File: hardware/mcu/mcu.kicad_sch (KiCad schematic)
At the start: 20 parts, among them J1 PROG, U1 RP2040, U3 W25Q32JVZP, Y1 ABLS

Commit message: library updates, mcu i2c devices
added MAX31331 RTC to library, added EEPROM and RTC sub-schematic to MCU, expanded mcu planning chart
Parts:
- added C14: 1u, Capacitor_SMD:C_0603_1608Metric_Pad1.08x0.95mm_HandSolder, symbol Device:C
- added R10: 100k, Resistor_SMD:R_0402_1005Metric_Pad0.72x0.64mm_HandSolder, symbol Device:R_US
- added R8, R9: 4.7k, Resistor_SMD:R_0402_1005Metric_Pad0.72x0.64mm_HandSolder, symbol Device:R_US
- added SW1: RESET, symbol Switch:SW_Push
- C1, C12, C2, C3, C4, C5, C6, C7, C8, C9: Size (none) -> 0402; VRating (none) -> 16V
- C10, C11: footprint Capacitor_SMD:C_0402_1005Metric_Pad0.74x0.62mm_HandSolder -> Capacitor_SMD:C_0603_1608Metric_Pad1.08x0.95mm_HandSolder; Size (none) -> 0603; VRating (none) -> 16V
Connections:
- net GND: now also C2.1, U1.19 (TESTEN), C14.2, SW1.1; no longer C2.2
- net VDD: now also C14.1, R10.2, R8.2, R9.2
- net XTL_2: now also C2.2; no longer C2.1
- net at U1.26 (RUN): now also R10.1, SW1.2
- net SW renamed SWD
- new net SCL: R9.1
- new net SDA: R8.1
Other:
- added sheet EEPROM-RTC (EEPROM-RTC.kicad_sch)

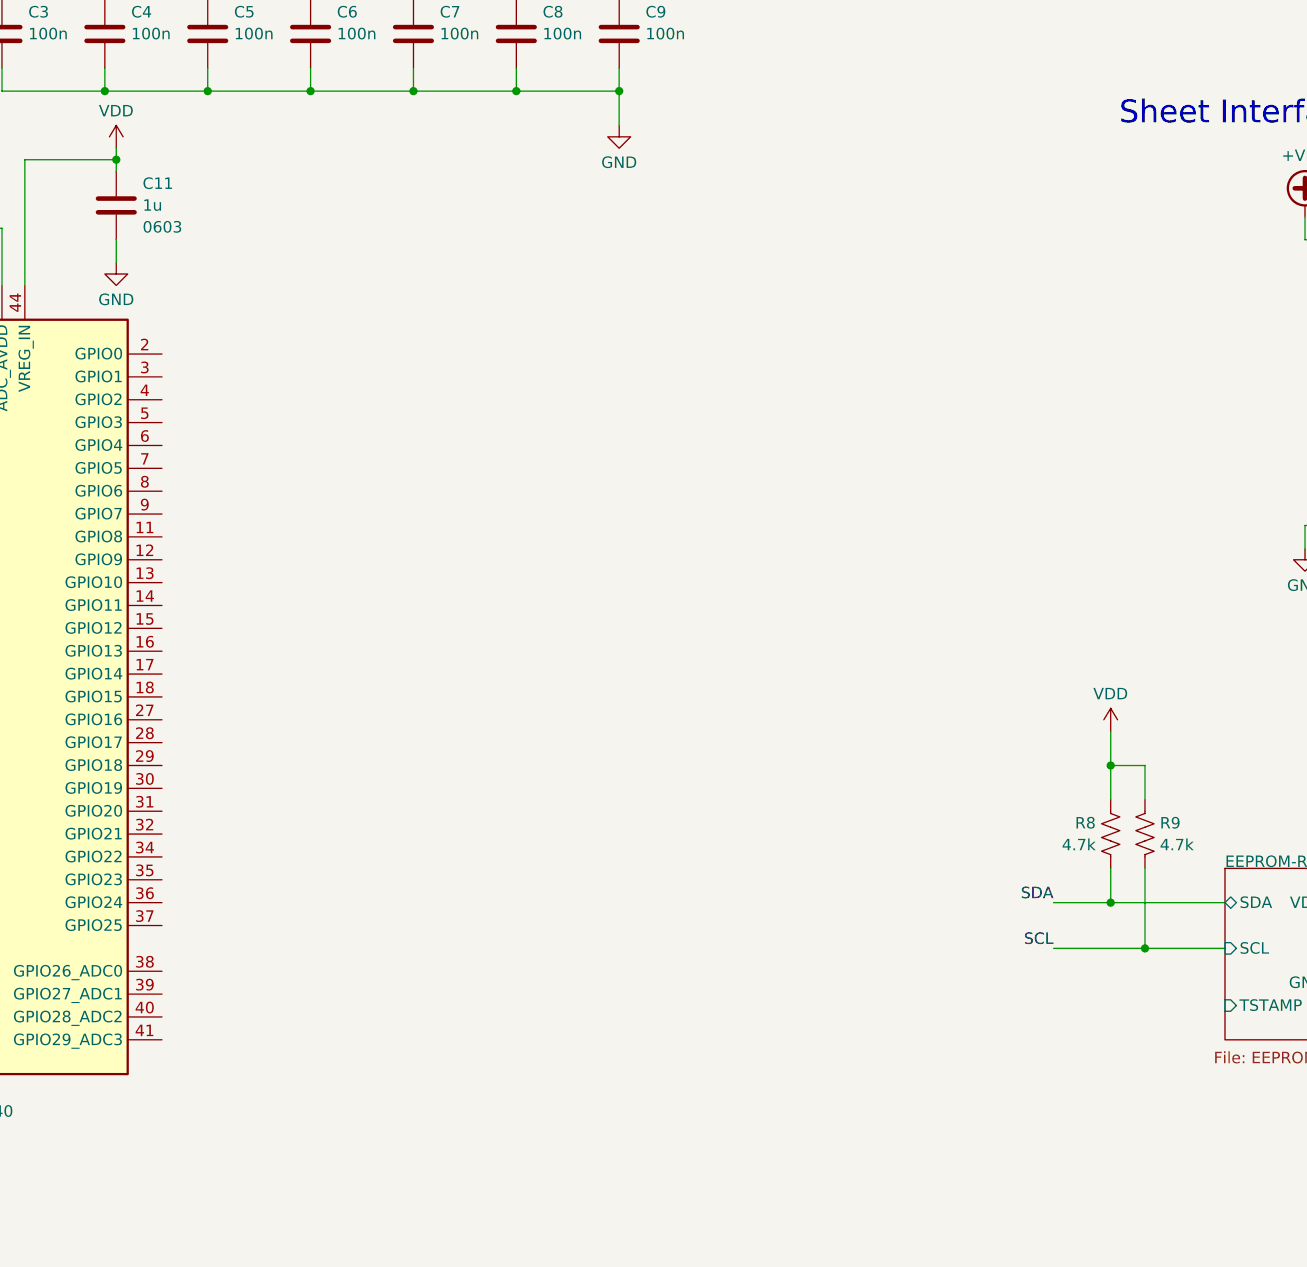
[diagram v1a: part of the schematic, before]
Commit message: I2C device notes
added notes on I2C device addresses (in-schematic)
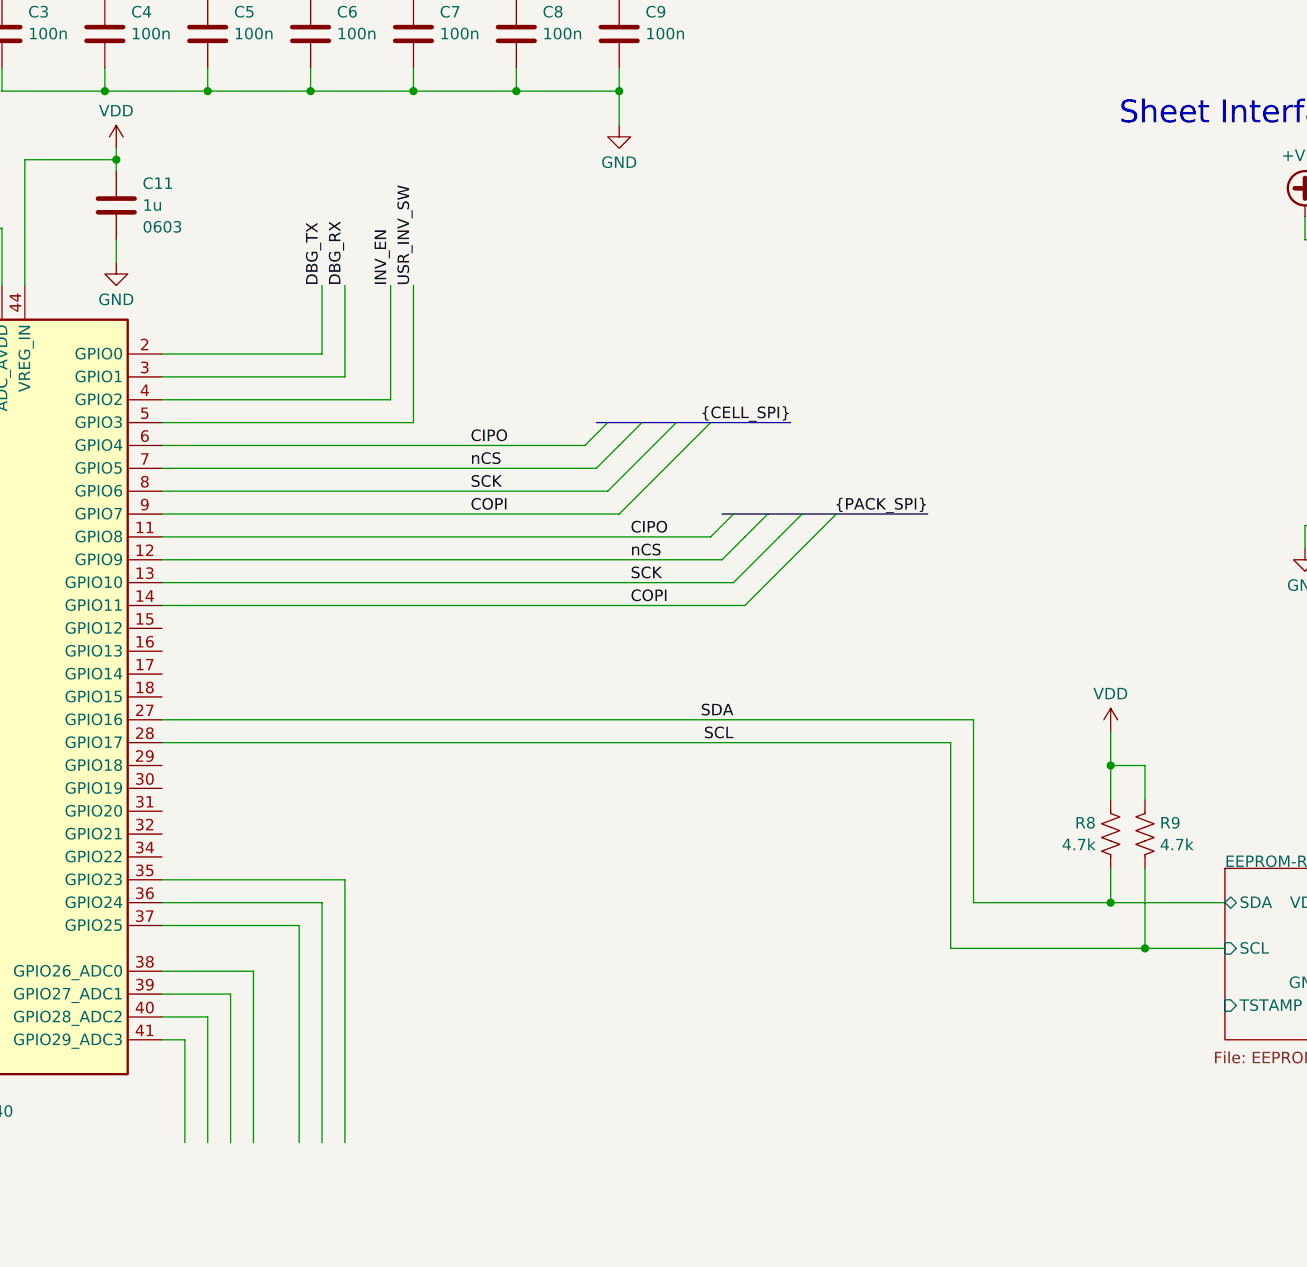
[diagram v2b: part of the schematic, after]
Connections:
- net SCL: now also U1.28 (GPIO17)
- net SDA: now also U1.27 (GPIO16)
- net CIPO: now reaches U1.11 (GPIO8)
- net CIPO: now also U1.6 (GPIO4)
- net nCS: now reaches U1.12 (GPIO9)
- net nCS: now also U1.7 (GPIO5)
- net SCK: now reaches U1.13 (GPIO10)
- net SCK: now also U1.8 (GPIO6)
- net COPI: now reaches U1.14 (GPIO11)
- net COPI: now also U1.9 (GPIO7)
- net DBG_TX: now reaches U1.2 (GPIO0)
- net DBG_RX: now reaches U1.3 (GPIO1)
- net INV_EN: now reaches U1.4 (GPIO2)
- net USR_INV_SW: now reaches U1.5 (GPIO3)

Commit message: huge update
massive update; finished lv power sys hardware design, started lv power sys mcu program
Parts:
- added J2: DEBUG, Connector_PinHeader_2.54mm:PinHeader_1x04_P2.54mm_Vertical, symbol Connector:Conn_01x04_Pin
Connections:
- net DBG_RX: now also J2.3 (Pin_3)
- net DBG_TX: now also J2.2 (Pin_2)
- net GND: now also J2.4 (Pin_4)
- net VDD: now also J2.1 (Pin_1)
- net CHG_SSR_EN: now reaches U1.15 (GPIO12)
- net BUS_SSR_EN: now reaches U1.16 (GPIO13)
- net BMS_PWR_EN: now reaches U1.17 (GPIO14)
- net MCU_RUN: now reaches R10.1, SW1.2, U1.26 (RUN)
- net LV_REG_EN: now reaches U1.29 (GPIO18)
- net TRICKLE_EN: now reaches U1.30 (GPIO19)
- net SUPV_DOUT: now reaches U1.31 (GPIO20)
- net SUPV_DIN: now reaches U1.32 (GPIO21)
- net SYS_LED: now reaches U1.34 (GPIO22)
- net USER_USB_DIR: now reaches U1.35 (GPIO23)
- net USB_BUS_EN: now reaches U1.36 (GPIO24)
- net USB_CC_DIR: now reaches U1.37 (GPIO25)
- net USBN: now reaches R4.2
- net USBP: now reaches R3.2
- no-connect marks 0 -> 1
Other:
- added sheet MCU_Power (MCU_Power.kicad_sch)
- moved on the sheet: J1, R3, R4, R8, R9
